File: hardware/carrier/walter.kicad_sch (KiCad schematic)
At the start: 21 parts, among them M1 Walter

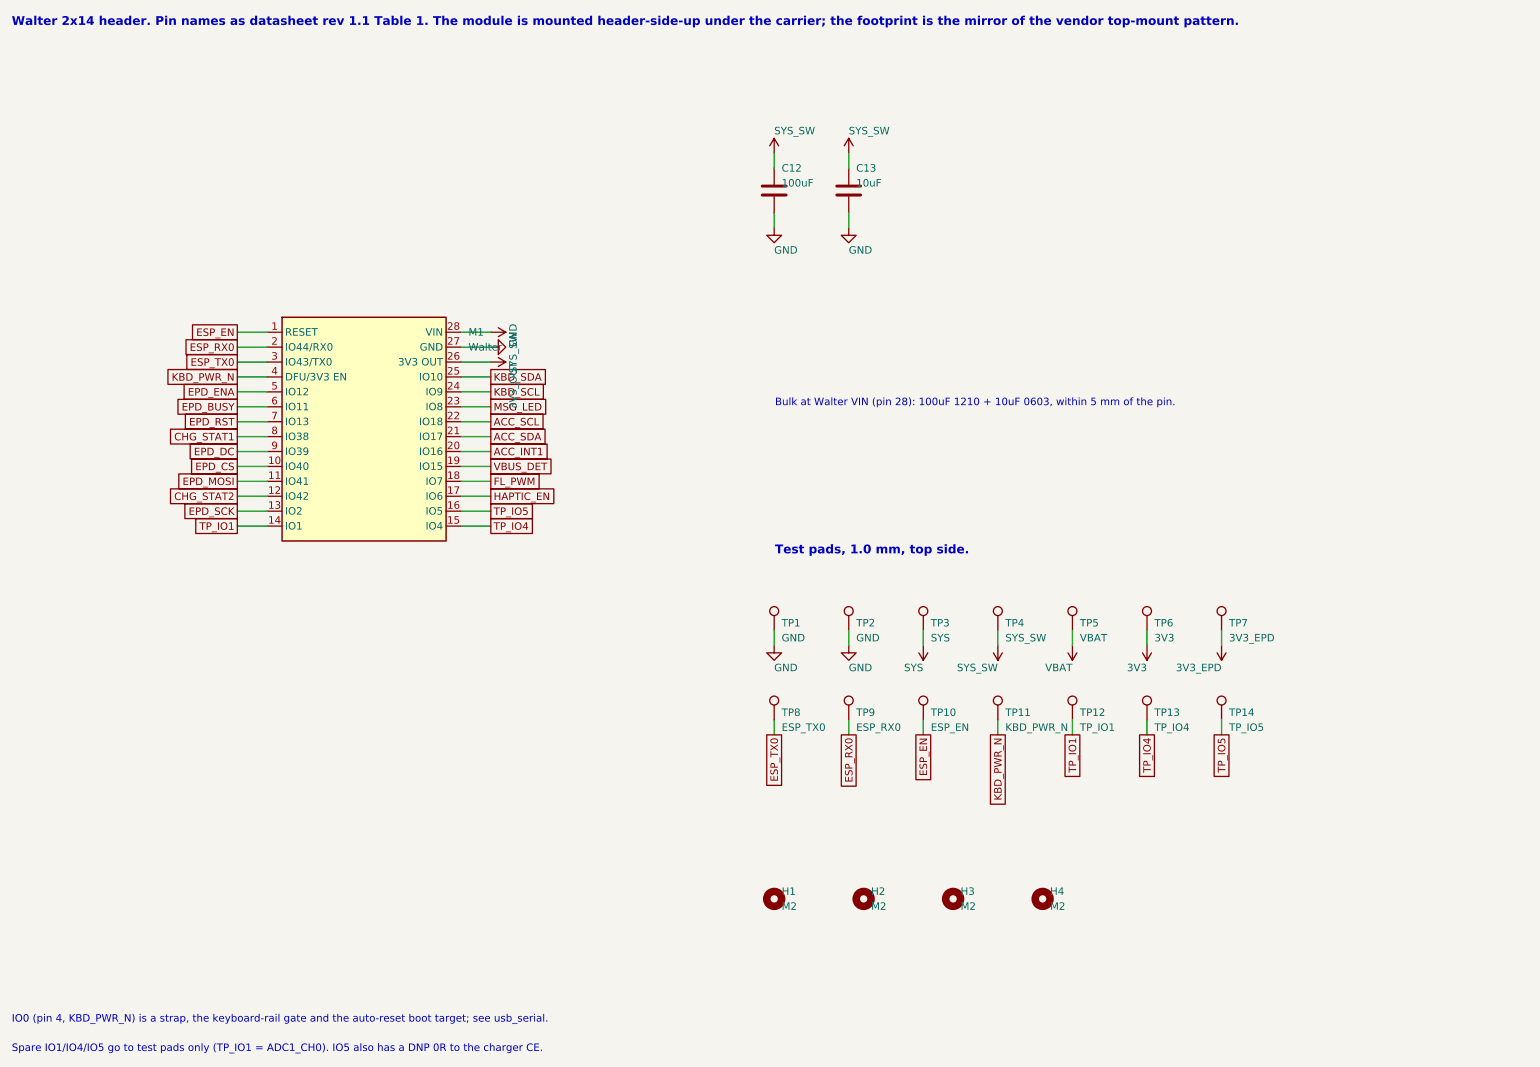
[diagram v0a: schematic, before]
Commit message: hardware/carrier: front light is the GDEY029T94-FL03 (6-pin flex -> FH34SRJ-6S on the panel board, anode/cathode over a 10-way SH cable, 33R 1206 + Q4 PWM drive replaces the NSI45020), front-light button SW2 on IO4 (FL_BTN), low-profile pass (FH34SRJ 1.0 mm ZIFs, 2 x 100uF 0805 instead of the 2.5 mm 1210, part-height table), sleep-current audit (Q1 gate pull-up 100k -> 2.2M: 38 -> 1.9 uA; SN74LVC2G126 moved to the bus-powered BRG_VDD rail: 0 on battery; table in the README), TPS62840 has no fixed-3.3 V variant (README). Custom FH34SRJ footprints from the Hirose catalog; LCSC numbers via the JLCPCB parts API. Both boards re-placed and re-routed: 0 unconnected, 0 clearance/courtyard errors, silk notes only; ERC 0/0; exports refreshed (owner, 17 Oct 2026)
Co-Authored-By: Claude Fable 5.1 <noreply@anthropic.com>
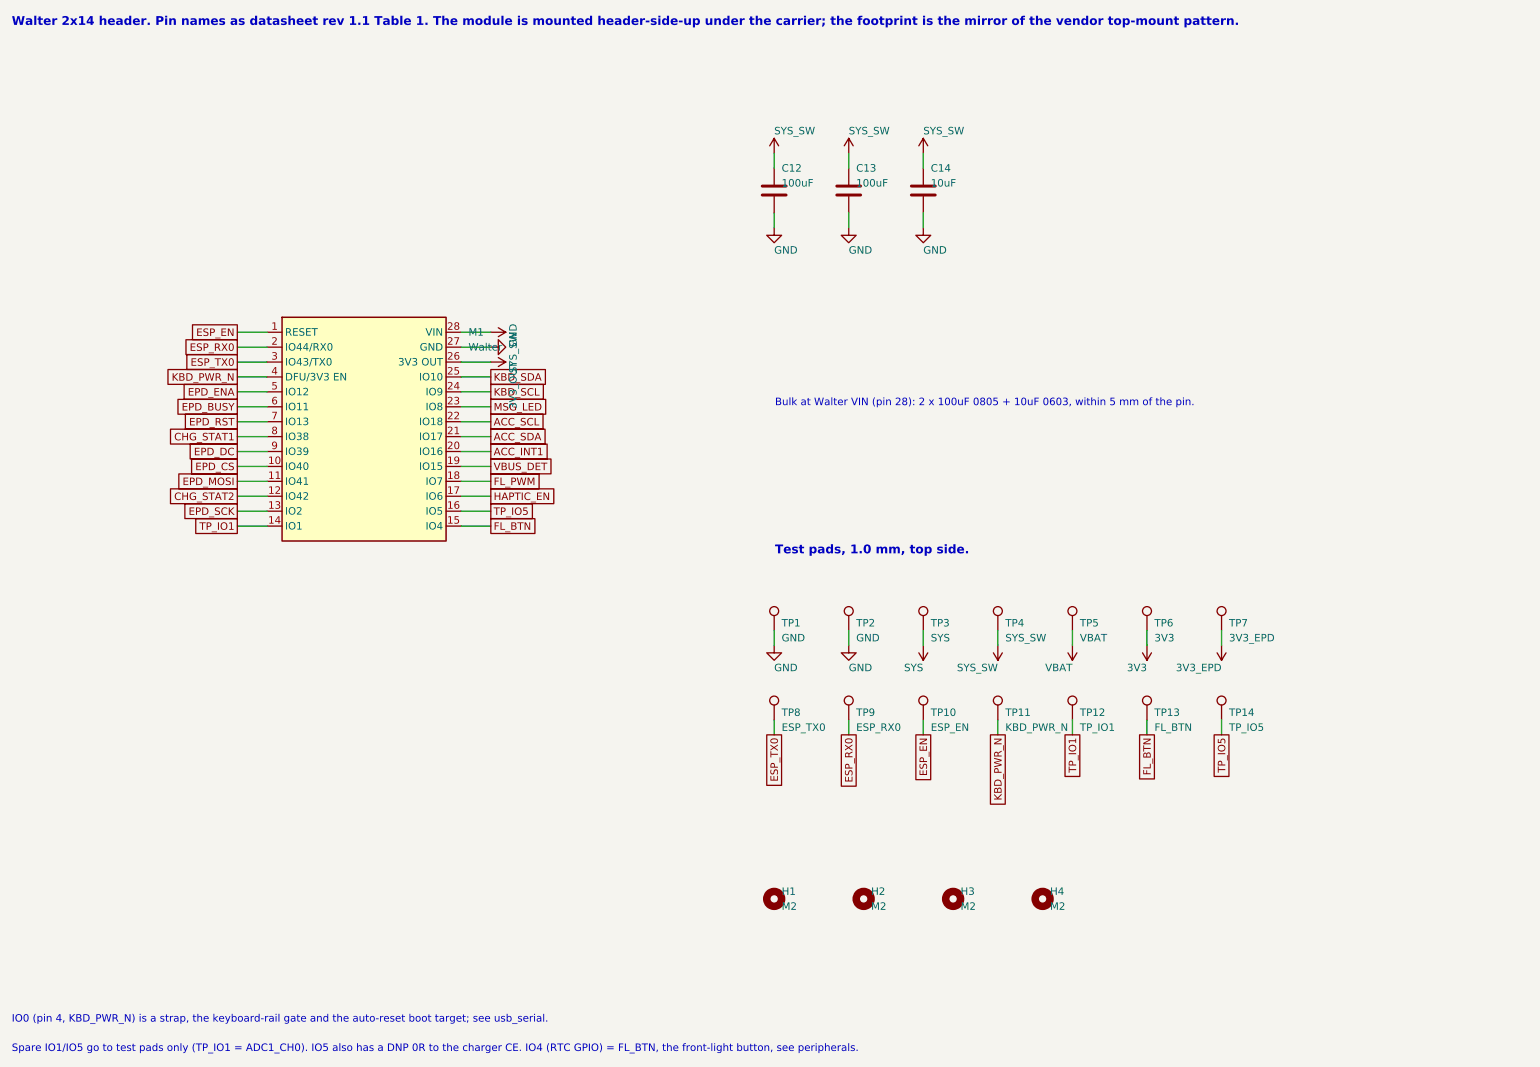
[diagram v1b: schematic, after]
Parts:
- added C14: 10uF, Capacitor_SMD:C_0603_1608Metric, symbol Device:C
- C12: footprint Capacitor_SMD:C_1210_3225Metric -> Capacitor_SMD:C_0805_2012Metric; LCSC C49066 -> C141660; MPN CL32A107MQVNNNE -> GRM21BR60J107ME15L; Note Walter VIN bulk; LTE burst -> Walter VIN bulk; LTE burst; 0805 1.25 mm tall (the 1210 was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
- C13: value 10uF -> 100uF; footprint Capacitor_SMD:C_0603_1608Metric -> Capacitor_SMD:C_0805_2012Metric; LCSC C19702 -> C141660; MPN CL10A106KP8NNNC -> GRM21BR60J107ME15L; Note (none) -> second 100uF makes up for 0805 DC bias loss
- TP13: value TP_IO4 -> FL_BTN
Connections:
- net GND: now also C14.2
- net SYS_SW: now also C14.1
- net TP_IO4 renamed FL_BTN
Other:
- note added: "Bulk at Walter VIN (pin 28): 2 x 100uF 0805 + 10uF 0603, within 5 mm of the pin."
- note added: "Spare IO1/IO5 go to test pads only (TP_IO1 = ADC1_CH0). IO5 also has a DNP 0R to the charger CE. IO4 (RTC GPIO) = FL_BTN, the front-light button, see peripherals."
- note removed: "Bulk at Walter VIN (pin 28): 100uF 1210 + 10uF 0603, within 5 mm of the pin."
- note removed: "Spare IO1/IO4/IO5 go to test pads only (TP_IO1 = ADC1_CH0). IO5 also has a DNP 0R to the charger CE."
